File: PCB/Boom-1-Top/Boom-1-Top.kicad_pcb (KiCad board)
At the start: 2 copper layers, 310 parts, among them J37 Osc1Conn, J38 Osc2Conn, J39 SubNoiseConn, J40 FiltConn2, J41 EnvGenConn2, J42 EnvGenConn1, J43 FXConn1, J44 FiltConn1, J45 FXConn2, J46 EnvGenConn3, SW1 Rotary_Encoder, SW10 Rotary_Encoder, SW11 Rotary_Encoder, SW12 Rotary_Encoder, SW13 Rotary_Encoder, SW14 Rotary_Encoder, SW15 Rotary_Encoder_Switch, SW16 Rotary_Encoder_Switch, SW17 Rotary_Encoder, SW18 Rotary_Encoder, SW19 Rotary_Encoder, SW2 Rotary_Encoder, SW20 Rotary_Encoder, SW21 Rotary_Encoder, SW22 Rotary_Encoder, SW23 Rotary_Encoder, SW24 Rotary_Encoder, SW25 Rotary_Encoder, SW26 Rotary_Encoder, SW27 Rotary_Encoder, SW28 Rotary_Encoder_Switch, SW29 Rotary_Encoder, SW3 Rotary_Encoder, SW30 Rotary_Encoder, SW31 Rotary_Encoder, SW32 Rotary_Encoder, SW33 Rotary_Encoder, SW34 Rotary_Encoder, SW35 Rotary_Encoder, SW36 Rotary_Encoder, SW37 Rotary_Encoder, SW38 Rotary_Encoder, SW39 Rotary_Encoder, SW4 Rotary_Encoder, SW40 Rotary_Encoder, SW5 Rotary_Encoder, SW6 Rotary_Encoder, SW7 Rotary_Encoder, SW8 Rotary_Encoder, SW9 Rotary_Encoder, U1 STM32F407VGTx, U10 DAC7678xPW, U11 PIC18F26Q43, U12 PIC18F26Q43, U13 PIC18F26Q43, U14 PIC18F26Q43, U15 PIC18F26Q43, U16 PIC18F26Q43, U17 PIC18F26Q43, U18 PIC18F26Q43, U19 PIC18F26Q43, U2 PIC18F26Q43, U20 PIC18F26Q43, U3 AD5290, U4 AD5290, U5 DAC7678xPW, U6 DAC7678xPW, U7 DAC7678xPW, U8 DAC7678xPW, U9 DAC7678xPW

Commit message: Schematic WIP
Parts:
- added C100: 100nF, Capacitor_SMD:C_0603_1608Metric, F.Cu at (426.1, 310.0)
- added C101: 100nF, Capacitor_SMD:C_0603_1608Metric, F.Cu at (417.0, 317.2)
- added C102: 10uF, Capacitor_SMD:C_0603_1608Metric, F.Cu at (422.0, 312.5)
- added C103: 100nF, Capacitor_SMD:C_0603_1608Metric, F.Cu at (393.8, 341.5)
- added C104: 100nF, Capacitor_SMD:C_0603_1608Metric, F.Cu at (431.3, 304.9)
- added C105: 100nF, Capacitor_SMD:C_0603_1608Metric, F.Cu at (401.2, 332.8)
- added C106: 10nF, Capacitor_SMD:C_0603_1608Metric, F.Cu at (397.8, 325.3)
- added C107: 100nF, Capacitor_SMD:C_0603_1608Metric, F.Cu at (409.0, 316.8)
- added C108: 100nF, Capacitor_SMD:C_0603_1608Metric, F.Cu at (397.8, 327.8)
- added C109: 100nF, Capacitor_SMD:C_0603_1608Metric, F.Cu at (385.8, 340.3)
- added C110: 100nF, Capacitor_SMD:C_0603_1608Metric, F.Cu at (423.3, 302.4)
- added C111: 100nF, Capacitor_SMD:C_0603_1608Metric, F.Cu at (401.8, 325.3)
- added C112: 100nF, Capacitor_SMD:C_0603_1608Metric, F.Cu at (423.3, 304.9)
- added C113: 100nF, Capacitor_SMD:C_0603_1608Metric, F.Cu at (401.8, 327.8)
- added C114: 100nF, Capacitor_SMD:C_0603_1608Metric, F.Cu at (397.8, 330.3)
- added C115: 100nF, Capacitor_SMD:C_0603_1608Metric, F.Cu at (409.0, 319.4)
- added C116: 100nF, Capacitor_SMD:C_0603_1608Metric, F.Cu at (418.1, 309.6)
- added C117: 100nF, Capacitor_SMD:C_0603_1608Metric, F.Cu at (414.0, 312.2)
- added C118: 100nF, Capacitor_SMD:C_0603_1608Metric, F.Cu at (391.8, 336.5)
- added C119: 100nF, Capacitor_SMD:C_0603_1608Metric, F.Cu at (414.0, 314.7)
- added C120: 100nF, Capacitor_SMD:C_0603_1608Metric, F.Cu at (427.3, 302.4)
- added C121: 100nF, Capacitor_SMD:C_0603_1608Metric, F.Cu at (389.8, 339.2)
- added C122: 100nF, Capacitor_SMD:C_0603_1608Metric, F.Cu at (405.9, 325.3)
- added C123: 100nF, Capacitor_SMD:C_0603_1608Metric, F.Cu at (418.0, 312.2)
- added C124: 100nF, Capacitor_SMD:C_0603_1608Metric, F.Cu at (409.0, 321.9)
- added C125: 100nF, Capacitor_SMD:C_0603_1608Metric, F.Cu at (397.2, 332.8)
- added C126: 100nF, Capacitor_SMD:C_0603_1608Metric, F.Cu at (423.3, 307.5)
- added C127: 100nF, Capacitor_SMD:C_0603_1608Metric, F.Cu at (427.3, 304.9)
- added C128: 100nF, Capacitor_SMD:C_0603_1608Metric, F.Cu at (389.8, 341.7)
- added C129: 100nF, Capacitor_SMD:C_0603_1608Metric, F.Cu at (413.0, 317.2)
- added C130: 100nF, Capacitor_SMD:C_0603_1608Metric, F.Cu at (401.8, 330.3)
- added C131: 100nF, Capacitor_SMD:C_0603_1608Metric, F.Cu at (405.9, 327.8)
- added C132: 100nF, Capacitor_SMD:C_0603_1608Metric, F.Cu at (413.0, 319.8)
- added C133: 100nF, Capacitor_SMD:C_0603_1608Metric, F.Cu at (422.1, 310.0)
- added C134: 100nF, Capacitor_SMD:C_0603_1608Metric, F.Cu at (397.2, 335.3)
- added C135: 100nF, Capacitor_SMD:C_0603_1608Metric, F.Cu at (418.0, 314.7)
- added C136: 100nF, Capacitor_SMD:C_0603_1608Metric, F.Cu at (393.8, 339.0)
- added C137: 100nF, Capacitor_SMD:C_0603_1608Metric, F.Cu at (431.3, 302.4)
- added C138: 100nF, Capacitor_SMD:C_0603_1608Metric, F.Cu at (409.9, 324.4)
- added C81: 100nF, Capacitor_SMD:C_0603_1608Metric, F.Cu at (433.1, 317.5)
- added C82: 10uF, Capacitor_SMD:C_0603_1608Metric, F.Cu at (417.9, 332.3)
- added C83: 100nF, Capacitor_SMD:C_0603_1608Metric, F.Cu at (429.9, 320.0)
- added C84: 10uF, Capacitor_SMD:C_0603_1608Metric, F.Cu at (421.9, 327.5)
- added C85: 12pF, Capacitor_SMD:C_0603_1608Metric, F.Cu at (409.8, 339.4)
- added C86: 2.2uF, Capacitor_SMD:C_0603_1608Metric, F.Cu at (413.9, 334.8)
- added C87: 100nF, Capacitor_SMD:C_0603_1608Metric, F.Cu at (413.9, 324.8)
- added C88: 12pF, Capacitor_SMD:C_0603_1608Metric, F.Cu at (431.3, 307.5)
- added C89: 100nF, Capacitor_SMD:C_0603_1608Metric, F.Cu at (426.0, 312.5)
- added C90: 10uF, Capacitor_SMD:C_0603_1608Metric, F.Cu at (405.2, 332.8)
- added C91: 100nF, Capacitor_SMD:C_0603_1608Metric, F.Cu at (397.8, 340.4)
- added C92: 100nF, Capacitor_SMD:C_0603_1608Metric, F.Cu at (413.9, 322.3)
- added C93: 10uF, Capacitor_SMD:C_0603_1608Metric, F.Cu at (435.3, 302.4)
- added C94: 100nF, Capacitor_SMD:C_0603_1608Metric, F.Cu at (397.8, 337.8)
- added C95: 2.2uF, Capacitor_SMD:C_0603_1608Metric, F.Cu at (422.0, 315.0)
- added C96: 100nF, Capacitor_SMD:C_0603_1608Metric, F.Cu at (401.2, 335.3)
- added C97: 10uF, Capacitor_SMD:C_0603_1608Metric, F.Cu at (417.0, 319.8)
- added C98: 100nF, Capacitor_SMD:C_0603_1608Metric, F.Cu at (409.9, 326.9)
- added C99: 2.2uF, Capacitor_SMD:C_0603_1608Metric, F.Cu at (405.9, 330.3)
- added D1: B5819W, Diode_SMD:D_SOD-123, F.Cu at (375.1, 338.2)
- added D2: Red, LED_SMD:LED_0603_1608Metric, F.Cu at (414.1, 309.7)
- added D3: 1N4148, Diode_SMD:D_SOD-123, F.Cu at (380.9, 340.7)
- added F1: 500mA, Fuse:Fuse_0603_1608Metric, F.Cu at (427.3, 307.5)
- added FB1: 100R@100Mhz, Inductor_SMD:L_0805_2012Metric, F.Cu at (387.6, 336.6)
- added FB2: 100R@100Mhz, Inductor_SMD:L_0805_2012Metric, F.Cu at (374.6, 341.3)
- added J1: DEBUG, Connector_PinHeader_1.27mm:PinHeader_2x05_P1.27mm_Vertical_SMD, F.Cu at (402.5, 305.4)
- added J10: MCLRCap, Connector_PinHeader_2.54mm:PinHeader_1x02_P2.54mm_Vertical, F.Cu at (393.5, 325.6)
- added J11: MCLRCap, Connector_PinHeader_2.54mm:PinHeader_1x02_P2.54mm_Vertical, F.Cu at (404.7, 312.0)
- added J12: MCLRCap, Connector_PinHeader_2.54mm:PinHeader_1x02_P2.54mm_Vertical, F.Cu at (382.9, 334.1)
- added J13: MCLRCap, Connector_PinHeader_2.54mm:PinHeader_1x02_P2.54mm_Vertical, F.Cu at (409.7, 303.5)
- added J14: MCLRCap, Connector_PinHeader_2.54mm:PinHeader_1x02_P2.54mm_Vertical, F.Cu at (400.0, 312.0)
- added J2: MIDI IN, 5PINDIN:SWITCHCRAFT_57PC5F, F.Cu at (388.3, 312.0)
- added J3: MIDI OUT, 5PINDIN:SWITCHCRAFT_57PC5F, F.Cu at (370.7, 312.0)
- added J4: MCLRCap, Connector_PinHeader_2.54mm:PinHeader_1x02_P2.54mm_Vertical, F.Cu at (387.6, 330.3)
- added J5: MCLRCap, Connector_PinHeader_2.54mm:PinHeader_1x02_P2.54mm_Vertical, F.Cu at (419.0, 303.5)
- added J6: MCLRCap, Connector_PinHeader_2.54mm:PinHeader_1x02_P2.54mm_Vertical, F.Cu at (404.7, 319.2)
- added J7: MCLRCap, Connector_PinHeader_2.54mm:PinHeader_1x02_P2.54mm_Vertical, F.Cu at (409.7, 310.7)
- added J8: MCLRCap, Connector_PinHeader_2.54mm:PinHeader_1x02_P2.54mm_Vertical, F.Cu at (400.0, 319.2)
- added J9: MCLRCap, Connector_PinHeader_2.54mm:PinHeader_1x02_P2.54mm_Vertical, F.Cu at (414.3, 303.5)
- added R161: 220R, Resistor_SMD:R_0603_1608Metric, F.Cu at (435.3, 304.9)
- added R162: 2.2K, Resistor_SMD:R_0603_1608Metric, F.Cu at (417.9, 322.3)
- added R163: 10K, Resistor_SMD:R_0603_1608Metric, F.Cu at (401.8, 337.8)
- added R164: 10K, Resistor_SMD:R_0603_1608Metric, F.Cu at (421.0, 317.5)
- added R165: 2.2K, Resistor_SMD:R_0603_1608Metric, F.Cu at (409.9, 329.4)
- added R166: 2.2K, Resistor_SMD:R_0603_1608Metric, F.Cu at (430.1, 310.0)
- added R167: 2.2K, Resistor_SMD:R_0603_1608Metric, F.Cu at (405.2, 335.3)
- added R168: 2.2K, Resistor_SMD:R_0603_1608Metric, F.Cu at (426.0, 315.0)
- added R169: 220R, Resistor_SMD:R_0603_1608Metric, F.Cu at (409.9, 331.9)
- added R170: 220R, Resistor_SMD:R_0603_1608Metric, F.Cu at (413.9, 327.3)
- added R171: 10K, Resistor_SMD:R_0603_1608Metric, F.Cu at (401.8, 340.4)
- added R172: 470R, Resistor_SMD:R_0603_1608Metric, F.Cu at (430.1, 312.5)
- added R173: 470R, Resistor_SMD:R_0603_1608Metric, F.Cu at (435.3, 307.5)
- added R174: 470R, Resistor_SMD:R_0603_1608Metric, F.Cu at (425.1, 317.5)
- added R175: 10K, Resistor_SMD:R_0603_1608Metric, F.Cu at (417.9, 324.8)
- added R176: 10K, Resistor_SMD:R_0603_1608Metric, F.Cu at (413.9, 329.8)
- added R177: 10K, Resistor_SMD:R_0603_1608Metric, F.Cu at (409.2, 334.4)
- added R178: 470R, Resistor_SMD:R_0603_1608Metric, F.Cu at (434.1, 310.0)
- added R179: 470R, Resistor_SMD:R_0603_1608Metric, F.Cu at (405.8, 337.8)
- added R180: 10K, Resistor_SMD:R_0603_1608Metric, F.Cu at (421.9, 320.0)
- added R181: 10K, Resistor_SMD:R_0603_1608Metric, F.Cu at (421.9, 322.5)
- added R182: 470R, Resistor_SMD:R_0603_1608Metric, F.Cu at (430.1, 315.0)
- added R183: 470R, Resistor_SMD:R_0603_1608Metric, F.Cu at (417.9, 327.3)
- added R184: 10K, Resistor_SMD:R_0603_1608Metric, F.Cu at (405.8, 340.4)
- added R185: 10K, Resistor_SMD:R_0603_1608Metric, F.Cu at (425.9, 320.0)
- added R186: 470R, Resistor_SMD:R_0603_1608Metric, F.Cu at (434.1, 312.5)
- added R187: 10K, Resistor_SMD:R_0603_1608Metric, F.Cu at (413.9, 332.3)
- added R188: 470R, Resistor_SMD:R_0603_1608Metric, F.Cu at (429.1, 317.5)
- added R189: 470R, Resistor_SMD:R_0603_1608Metric, F.Cu at (417.9, 329.8)
- added R190: 10K, Resistor_SMD:R_0603_1608Metric, F.Cu at (421.9, 325.0)
- added R191: 10K, Resistor_SMD:R_0603_1608Metric, F.Cu at (409.8, 336.9)
- added R192: 470R, Resistor_SMD:R_0603_1608Metric, F.Cu at (425.9, 322.5)
- added R193: 10K, Resistor_SMD:R_0603_1608Metric, F.Cu at (434.1, 315.0)
- added SW41: Reset, Button_Switch_THT:SW_PUSH_6mm, F.Cu at (375.3, 325.3)
- added U21: AMS1117-3.3, Package_TO_SOT_SMD:SOT-223-3_TabPin2, F.Cu at (367.4, 339.1)
- added U22: 6N137, Package_DIP:DIP-8_W7.62mm, F.Cu at (364.1, 325.3)
- added U3: AD5290, Package_SO:MSOP-10_3x3mm_P0.5mm, F.Cu at (387.5, 325.6)
- added U4: AD5290, Package_SO:MSOP-10_3x3mm_P0.5mm, F.Cu at (376.9, 334.2)
- added Y1: 16Mhz, Crystal:Crystal_SMD_3225-4Pin_3.2x2.5mm, F.Cu at (392.6, 332.7)
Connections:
- U1 pad 10: Net-(U1-Pad10) -> GND
- U1 pad 100: Net-(U1-Pad100) -> +3V3
- U1 pad 11: Net-(U1-Pad11) -> +3V3
- U1 pad 12: Net-(U1-Pad12) -> HSE_IN
- U1 pad 13: Net-(U1-Pad13) -> HSE_OUT
- U1 pad 19: Net-(U1-Pad19) -> +3V3
- U1 pad 20: Net-(U1-Pad20) -> GND
- U1 pad 21: Net-(U1-Pad21) -> +3.3VA
- U1 pad 22: Net-(U1-Pad22) -> +3.3VA
- U1 pad 27: Net-(U1-Pad27) -> GND
- U1 pad 28: Net-(U1-Pad28) -> +3V3
- U1 pad 37: Net-(U1-Pad37) -> BOOT1
- U1 pad 50: Net-(U1-Pad50) -> +3V3
- U1 pad 6: Net-(U1-Pad6) -> +3V3
- U1 pad 72: Net-(U1-Pad72) -> SWDIO
- U1 pad 74: Net-(U1-Pad74) -> GND
- U1 pad 75: Net-(U1-Pad75) -> +3V3
- U1 pad 76: Net-(U1-Pad76) -> SWCLK
- U1 pad 89: Net-(U1-Pad89) -> SWO
- U1 pad 94: Net-(U1-Pad94) -> BOOT0
- U1 pad 99: Net-(U1-Pad99) -> GND
- U11 pad 19: Net-(U11-Pad19) -> GND
- U11 pad 20: Net-(U11-Pad20) -> +5V
- U11 pad 8: Net-(U11-Pad8) -> GND
- U12 pad 19: Net-(U12-Pad19) -> GND
- U12 pad 20: Net-(U12-Pad20) -> +5V
- U12 pad 8: Net-(U12-Pad8) -> GND
- U13 pad 19: Net-(U13-Pad19) -> GND
- U13 pad 20: Net-(U13-Pad20) -> +5V
- U13 pad 8: Net-(U13-Pad8) -> GND
- U14 pad 19: Net-(U14-Pad19) -> GND
- U14 pad 20: Net-(U14-Pad20) -> +5V
- U14 pad 8: Net-(U14-Pad8) -> GND
- U15 pad 19: Net-(U15-Pad19) -> GND
- U15 pad 20: Net-(U15-Pad20) -> +5V
- U15 pad 8: Net-(U15-Pad8) -> GND
- U16 pad 19: Net-(U16-Pad19) -> GND
- U16 pad 20: Net-(U16-Pad20) -> +5V
- U16 pad 8: Net-(U16-Pad8) -> GND
- U17 pad 19: Net-(U17-Pad19) -> GND
- U17 pad 20: Net-(U17-Pad20) -> +5V
- U17 pad 8: Net-(U17-Pad8) -> GND
- U18 pad 19: Net-(U18-Pad19) -> GND
- U18 pad 20: Net-(U18-Pad20) -> +5V
- U18 pad 8: Net-(U18-Pad8) -> GND
- U19 pad 19: Net-(U19-Pad19) -> GND
- U19 pad 20: Net-(U19-Pad20) -> +5V
- U19 pad 8: Net-(U19-Pad8) -> GND
- U2 pad 19: Net-(U2-Pad19) -> GND
- U2 pad 20: Net-(U2-Pad20) -> +5V
- U2 pad 8: Net-(U2-Pad8) -> GND
- U20 pad 19: Net-(U20-Pad19) -> GND
- U20 pad 20: Net-(U20-Pad20) -> +5V
- U20 pad 8: Net-(U20-Pad8) -> GND
- U5 pad 15: I2CBus1SDA -> I2CBus1SCL
- U5 pad 16: I2CBus1SCL -> Net-(U5-Pad16)

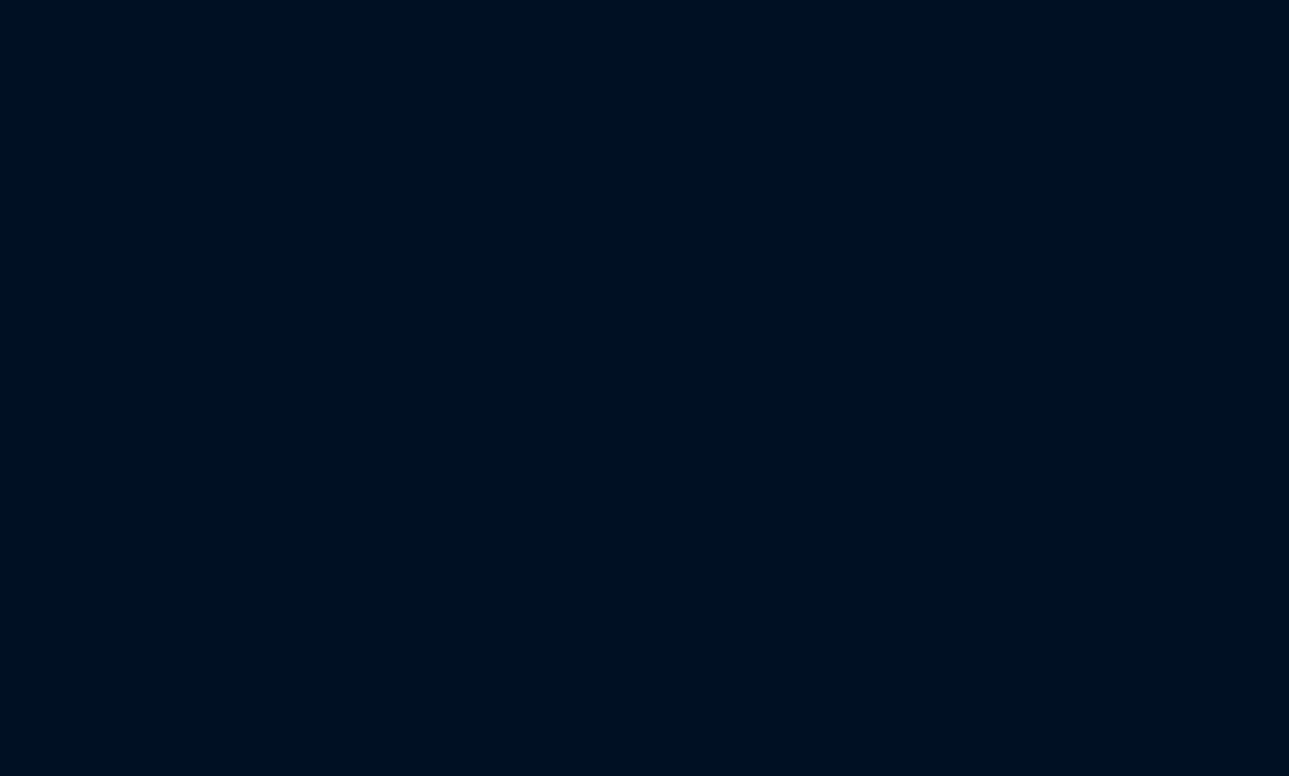
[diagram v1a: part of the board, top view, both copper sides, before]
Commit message: Annotated, set foot prints and updated PCB
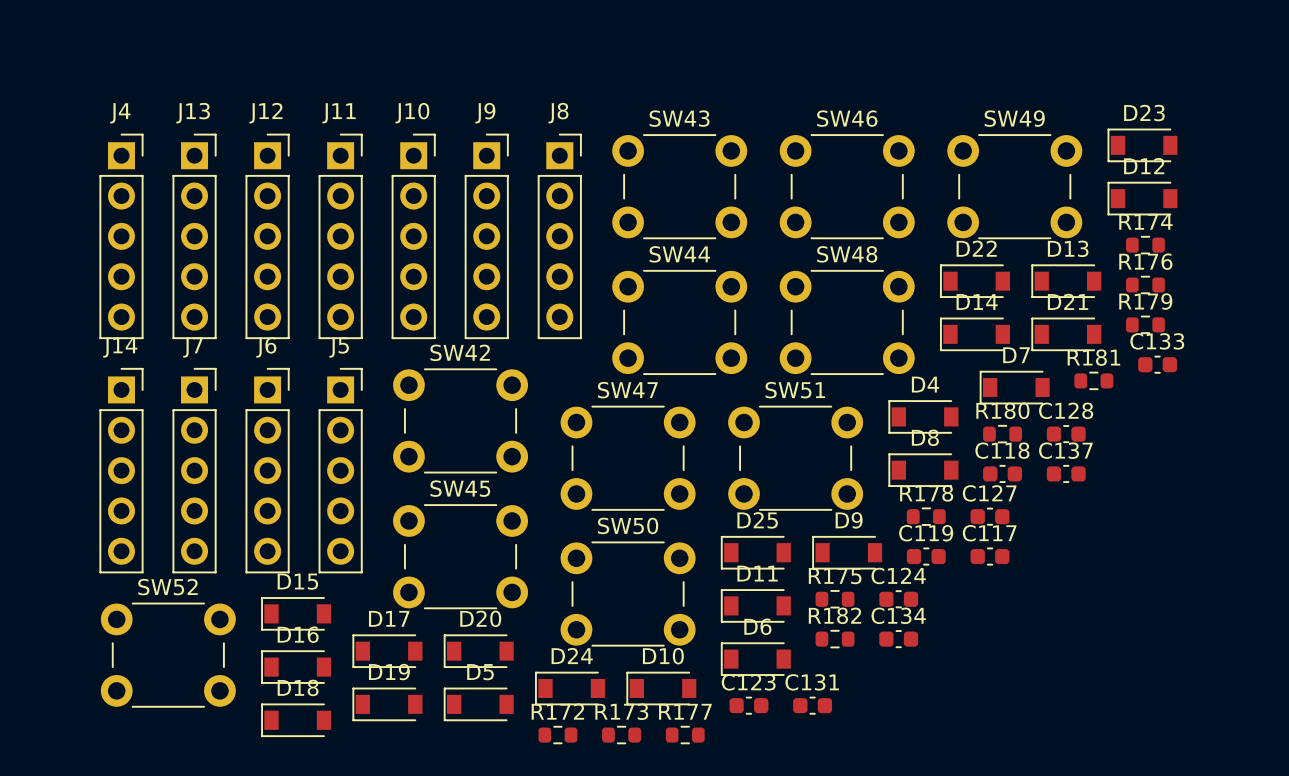
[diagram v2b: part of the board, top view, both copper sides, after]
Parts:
- added C117: 100nF, Capacitor_SMD:C_0603_1608Metric, F.Cu at (325.1, 365.8)
- added C118: 100nF, Capacitor_SMD:C_0603_1608Metric, F.Cu at (325.9, 360.6)
- added C119: 100nF, Capacitor_SMD:C_0603_1608Metric, F.Cu at (321.1, 365.8)
- added C123: 100nF, Capacitor_SMD:C_0603_1608Metric, F.Cu at (309.9, 375.1)
- added C124: 100nF, Capacitor_SMD:C_0603_1608Metric, F.Cu at (319.4, 368.4)
- added C127: 100nF, Capacitor_SMD:C_0603_1608Metric, F.Cu at (325.1, 363.2)
- added C128: 100nF, Capacitor_SMD:C_0603_1608Metric, F.Cu at (329.9, 358.1)
- added C131: 100nF, Capacitor_SMD:C_0603_1608Metric, F.Cu at (313.9, 375.1)
- added C133: 100nF, Capacitor_SMD:C_0603_1608Metric, F.Cu at (335.7, 353.7)
- added C134: 100nF, Capacitor_SMD:C_0603_1608Metric, F.Cu at (319.4, 371.0)
- added C137: 100nF, Capacitor_SMD:C_0603_1608Metric, F.Cu at (329.9, 360.6)
- added D10: B5819W, Diode_SMD:D_SOD-123, F.Cu at (304.5, 374.1)
- added D11: B5819W, Diode_SMD:D_SOD-123, F.Cu at (310.5, 368.9)
- added D12: B5819W, Diode_SMD:D_SOD-123, F.Cu at (334.8, 343.2)
- added D13: B5819W, Diode_SMD:D_SOD-123, F.Cu at (330.0, 348.4)
- added D14: B5819W, Diode_SMD:D_SOD-123, F.Cu at (324.3, 351.8)
- added D15: B5819W, Diode_SMD:D_SOD-123, F.Cu at (281.5, 369.4)
- added D16: B5819W, Diode_SMD:D_SOD-123, F.Cu at (281.5, 372.7)
- added D17: B5819W, Diode_SMD:D_SOD-123, F.Cu at (287.3, 371.7)
- added D18: B5819W, Diode_SMD:D_SOD-123, F.Cu at (281.5, 376.1)
- added D19: B5819W, Diode_SMD:D_SOD-123, F.Cu at (287.3, 375.1)
- added D20: B5819W, Diode_SMD:D_SOD-123, F.Cu at (293.0, 371.7)
- added D21: B5819W, Diode_SMD:D_SOD-123, F.Cu at (330.0, 351.8)
- added D22: B5819W, Diode_SMD:D_SOD-123, F.Cu at (324.3, 348.4)
- added D23: B5819W, Diode_SMD:D_SOD-123, F.Cu at (334.8, 339.9)
- added D24: B5819W, Diode_SMD:D_SOD-123, F.Cu at (298.8, 374.1)
- added D25: B5819W, Diode_SMD:D_SOD-123, F.Cu at (310.5, 365.5)
- added D4: B5819W, Diode_SMD:D_SOD-123, F.Cu at (321.0, 357.0)
- added D5: B5819W, Diode_SMD:D_SOD-123, F.Cu at (293.0, 375.1)
- added D6: B5819W, Diode_SMD:D_SOD-123, F.Cu at (310.5, 372.2)
- added D7: B5819W, Diode_SMD:D_SOD-123, F.Cu at (326.8, 355.1)
- added D8: B5819W, Diode_SMD:D_SOD-123, F.Cu at (321.0, 360.3)
- added D9: B5819W, Diode_SMD:D_SOD-123, F.Cu at (316.2, 365.5)
- added J10: PIC_DEBUG, Connector_PinSocket_2.54mm:PinSocket_1x05_P2.54mm_Vertical, F.Cu at (288.8, 340.5)
- added J11: PIC_DEBUG, Connector_PinSocket_2.54mm:PinSocket_1x05_P2.54mm_Vertical, F.Cu at (284.2, 340.5)
- added J12: PIC_DEBUG, Connector_PinSocket_2.54mm:PinSocket_1x05_P2.54mm_Vertical, F.Cu at (279.6, 340.5)
- added J13: PIC_DEBUG, Connector_PinSocket_2.54mm:PinSocket_1x05_P2.54mm_Vertical, F.Cu at (275.0, 340.5)
- added J14: PIC_DEBUG, Connector_PinSocket_2.54mm:PinSocket_1x05_P2.54mm_Vertical, F.Cu at (270.4, 355.3)
- added J4: PIC_DEBUG, Connector_PinSocket_2.54mm:PinSocket_1x05_P2.54mm_Vertical, F.Cu at (270.4, 340.5)
- added J5: PIC_DEBUG, Connector_PinSocket_2.54mm:PinSocket_1x05_P2.54mm_Vertical, F.Cu at (284.2, 355.3)
- added J6: PIC_DEBUG, Connector_PinSocket_2.54mm:PinSocket_1x05_P2.54mm_Vertical, F.Cu at (279.6, 355.3)
- added J7: PIC_DEBUG, Connector_PinSocket_2.54mm:PinSocket_1x05_P2.54mm_Vertical, F.Cu at (275.0, 355.3)
- added J8: PIC_DEBUG, Connector_PinSocket_2.54mm:PinSocket_1x05_P2.54mm_Vertical, F.Cu at (298.0, 340.5)
- added J9: PIC_DEBUG, Connector_PinSocket_2.54mm:PinSocket_1x05_P2.54mm_Vertical, F.Cu at (293.4, 340.5)
- added R172: 10K, Resistor_SMD:R_0603_1608Metric, F.Cu at (297.9, 377.0)
- added R173: 10K, Resistor_SMD:R_0603_1608Metric, F.Cu at (301.9, 377.0)
- added R174: 10K, Resistor_SMD:R_0603_1608Metric, F.Cu at (334.9, 346.1)
- added R175: 10K, Resistor_SMD:R_0603_1608Metric, F.Cu at (315.4, 368.4)
- added R176: 10K, Resistor_SMD:R_0603_1608Metric, F.Cu at (334.9, 348.7)
- added R177: 10K, Resistor_SMD:R_0603_1608Metric, F.Cu at (305.9, 377.0)
- added R178: 10K, Resistor_SMD:R_0603_1608Metric, F.Cu at (321.1, 363.2)
- added R179: 10K, Resistor_SMD:R_0603_1608Metric, F.Cu at (334.9, 351.2)
- added R180: 10K, Resistor_SMD:R_0603_1608Metric, F.Cu at (325.9, 358.1)
- added R181: 10K, Resistor_SMD:R_0603_1608Metric, F.Cu at (331.7, 354.7)
- added R182: 10K, Resistor_SMD:R_0603_1608Metric, F.Cu at (315.4, 371.0)
- added SW42: Reset, Button_Switch_THT:SW_PUSH_6mm, F.Cu at (288.5, 355.0)
- added SW43: Reset, Button_Switch_THT:SW_PUSH_6mm, F.Cu at (302.3, 340.2)
- added SW44: Reset, Button_Switch_THT:SW_PUSH_6mm, F.Cu at (302.3, 348.8)
- added SW45: Reset, Button_Switch_THT:SW_PUSH_6mm, F.Cu at (288.5, 363.5)
- added SW46: Reset, Button_Switch_THT:SW_PUSH_6mm, F.Cu at (312.9, 340.2)
- added SW47: Reset, Button_Switch_THT:SW_PUSH_6mm, F.Cu at (299.1, 357.3)
- added SW48: Reset, Button_Switch_THT:SW_PUSH_6mm, F.Cu at (312.9, 348.8)
- added SW49: Reset, Button_Switch_THT:SW_PUSH_6mm, F.Cu at (323.4, 340.2)
- added SW50: Reset, Button_Switch_THT:SW_PUSH_6mm, F.Cu at (299.1, 365.9)
- added SW51: Reset, Button_Switch_THT:SW_PUSH_6mm, F.Cu at (309.6, 357.3)
- added SW52: Reset, Button_Switch_THT:SW_PUSH_6mm, F.Cu at (270.1, 369.7)
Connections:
- R102 pad 1: Net-(R102-Pad1) -> +5V
- R58 pad 1: Net-(R58-Pad1) -> +5V
- R78 pad 1: Net-(R78-Pad1) -> +5V
- R86 pad 1: Net-(R86-Pad1) -> +5V
- SW15 pad S1: Net-(SW15-PadS1) -> GND
- SW16 pad S1: Net-(SW16-PadS1) -> GND
- SW28 pad S2: Net-(SW28-PadS2) -> GND
- U1 pad 25: Net-(U1-Pad25) -> MIDITXUSART
- U1 pad 30: Net-(U1-Pad30) -> SPIBus1CLK
- U1 pad 31: Net-(U1-Pad31) -> SPIBus1SDO
- U1 pad 32: Net-(U1-Pad32) -> SPIBus1SDI
- U1 pad 33: Net-(U1-Pad33) -> Osc1ScaleDPotCS
- U1 pad 34: Net-(U1-Pad34) -> Osc2ScaleDPotCS
- U1 pad 40: Net-(U1-Pad40) -> Osc1TuningOut
- U1 pad 42: Net-(U1-Pad42) -> Osc2TuningOut
- U1 pad 47: Net-(U1-Pad47) -> I2CBus2SCL
- U1 pad 48: Net-(U1-Pad48) -> I2CBus2SDA
- U1 pad 55: Net-(U1-Pad55) -> SubAmpEnvGate
- U1 pad 56: Net-(U1-Pad56) -> SubAmpEnvTrigger
- U1 pad 57: Net-(U1-Pad57) -> OscFiltEnv2Gate
- U1 pad 58: Net-(U1-Pad58) -> OscFiltEnv2Trigger
- U1 pad 59: Net-(U1-Pad59) -> OscFiltEnv1Gate
- U1 pad 60: Net-(U1-Pad60) -> OscFiltEnv1Trigger
- U1 pad 87: Net-(U1-Pad87) -> MIDIRXUSART
- U1 pad 92: Net-(U1-Pad92) -> I2CBus1SCL
- U1 pad 93: Net-(U1-Pad93) -> I2CBus1SDA
- U11 pad 1: Net-(R173-Pad2) -> Net-(D5-Pad1)
- U11 pad 15: Net-(U11-Pad15) -> Net-(C7-Pad2)
- U11 pad 16: Net-(U11-Pad16) -> Net-(C8-Pad1)
- U11 pad 17: Net-(U11-Pad17) -> Net-(C9-Pad2)
- U11 pad 18: Net-(U11-Pad18) -> Net-(C10-Pad1)
- U11 pad 2: Net-(U11-Pad2) -> Net-(C5-Pad2)
- U11 pad 21: Net-(U11-Pad21) -> I2CBus1SCL
- U11 pad 22: Net-(U11-Pad22) -> I2CBus1SDA
- U11 pad 3: Net-(U11-Pad3) -> Net-(C6-Pad1)
- U11 pad 4: Net-(U11-Pad4) -> Net-(C17-Pad2)
- U11 pad 5: Net-(U11-Pad5) -> Net-(C18-Pad1)
- U12 pad 1: Net-(R174-Pad2) -> Net-(D9-Pad1)
- U12 pad 15: Net-(U12-Pad15) -> Net-(C13-Pad2)
- U12 pad 16: Net-(U12-Pad16) -> Net-(C14-Pad1)
- U12 pad 2: Net-(U12-Pad2) -> Net-(C11-Pad2)
- U12 pad 21: Net-(U12-Pad21) -> I2CBus1SCL
- U12 pad 22: Net-(U12-Pad22) -> I2CBus1SDA
- U12 pad 3: Net-(U12-Pad3) -> Net-(C12-Pad1)
- U12 pad 4: Net-(U12-Pad4) -> Net-(C20-Pad1)
- U12 pad 5: Net-(U12-Pad5) -> Net-(C19-Pad2)
- U13 pad 1: Net-(R178-Pad2) -> Net-(D11-Pad1)
- U13 pad 15: Net-(U13-Pad15) -> Net-(C36-Pad2)
- U13 pad 16: Net-(U13-Pad16) -> Net-(C33-Pad1)
- U13 pad 2: Net-(U13-Pad2) -> Net-(C23-Pad2)
- U13 pad 21: Net-(U13-Pad21) -> I2CBus1SCL
- U13 pad 22: Net-(U13-Pad22) -> I2CBus1SDA
- U13 pad 3: Net-(U13-Pad3) -> Net-(C24-Pad1)
- U13 pad 4: Net-(U13-Pad4) -> Net-(C49-Pad2)
- U13 pad 5: Net-(U13-Pad5) -> Net-(C47-Pad1)
- U14 pad 1: Net-(R179-Pad2) -> Net-(D14-Pad1)
- U14 pad 15: Net-(U14-Pad15) -> Net-(C37-Pad2)
- U14 pad 16: Net-(U14-Pad16) -> Net-(C34-Pad1)
- U14 pad 17: Net-(U14-Pad17) -> Net-(C55-Pad2)
- U14 pad 18: Net-(U14-Pad18) -> Net-(C56-Pad1)
- U14 pad 2: Net-(U14-Pad2) -> Net-(C25-Pad2)
- U14 pad 21: Net-(U14-Pad21) -> I2CBus1SCL
- U14 pad 22: Net-(U14-Pad22) -> I2CBus1SDA
- U14 pad 3: Net-(U14-Pad3) -> Net-(C26-Pad1)
- U14 pad 4: Net-(U14-Pad4) -> Net-(C50-Pad2)
- U14 pad 5: Net-(U14-Pad5) -> Net-(C48-Pad1)
- U14 pad 9: Net-(U14-Pad9) -> Net-(SW28-PadS1)
- U15 pad 1: Net-(R182-Pad2) -> Net-(D15-Pad1)
- U15 pad 15: Net-(U15-Pad15) -> Net-(C41-Pad2)
- U15 pad 16: Net-(U15-Pad16) -> Net-(C39-Pad1)
- U15 pad 17: Net-(U15-Pad17) -> Net-(C53-Pad2)
- U15 pad 18: Net-(U15-Pad18) -> Net-(C51-Pad1)
- U15 pad 2: Net-(U15-Pad2) -> Net-(C31-Pad2)
- U15 pad 21: Net-(U15-Pad21) -> I2CBus1SCL
- U15 pad 22: Net-(U15-Pad22) -> I2CBus1SDA
- U15 pad 3: Net-(U15-Pad3) -> Net-(C29-Pad1)
- U15 pad 4: Net-(U15-Pad4) -> Net-(C45-Pad2)
- U15 pad 5: Net-(U15-Pad5) -> Net-(C43-Pad1)
- U15 pad 9: Net-(U15-Pad9) -> Net-(SW15-PadS2)
- U16 pad 1: Net-(R183-Pad2) -> Net-(D17-Pad1)
- U16 pad 15: Net-(U16-Pad15) -> Net-(C42-Pad2)
- U16 pad 16: Net-(U16-Pad16) -> Net-(C40-Pad1)
- U16 pad 17: Net-(U16-Pad17) -> Net-(C54-Pad2)
- U16 pad 18: Net-(U16-Pad18) -> Net-(C52-Pad1)
- U16 pad 2: Net-(U16-Pad2) -> Net-(C32-Pad2)
- U16 pad 21: Net-(U16-Pad21) -> I2CBus2SCL
- U16 pad 22: Net-(U16-Pad22) -> I2CBus2SDA
- U16 pad 3: Net-(U16-Pad3) -> Net-(C30-Pad1)
- U16 pad 4: Net-(U16-Pad4) -> Net-(C46-Pad2)
- U16 pad 5: Net-(U16-Pad5) -> Net-(C44-Pad1)
- U16 pad 9: Net-(U16-Pad9) -> Net-(SW16-PadS2)
- U17 pad 1: Net-(R186-Pad2) -> Net-(D19-Pad1)
- U17 pad 15: Net-(U17-Pad15) -> Net-(C35-Pad2)
- U17 pad 16: Net-(U17-Pad16) -> Net-(C38-Pad1)
- U17 pad 2: Net-(U17-Pad2) -> Net-(C27-Pad2)
- U17 pad 21: Net-(U17-Pad21) -> I2CBus2SCL
- U17 pad 22: Net-(U17-Pad22) -> I2CBus2SDA
- U17 pad 3: Net-(U17-Pad3) -> Net-(C28-Pad1)
- U18 pad 1: Net-(R188-Pad2) -> Net-(D24-Pad1)
- U18 pad 15: Net-(U18-Pad15) -> Net-(C62-Pad2)
- U18 pad 16: Net-(U18-Pad16) -> Net-(C65-Pad1)
- U18 pad 17: Net-(U18-Pad17) -> Net-(C75-Pad2)
- U18 pad 18: Net-(U18-Pad18) -> Net-(C77-Pad1)
- U18 pad 2: Net-(U18-Pad2) -> Net-(C57-Pad2)
- U18 pad 21: Net-(U18-Pad21) -> I2CBus2SCL
- U18 pad 22: Net-(U18-Pad22) -> I2CBus2SDA
- U18 pad 3: Net-(U18-Pad3) -> Net-(C59-Pad1)
- U18 pad 4: Net-(U18-Pad4) -> Net-(C69-Pad2)
- U18 pad 5: Net-(U18-Pad5) -> Net-(C72-Pad1)
- U19 pad 1: Net-(R189-Pad2) -> Net-(D23-Pad1)
- U19 pad 15: Net-(U19-Pad15) -> Net-(C66-Pad2)
- U19 pad 16: Net-(U19-Pad16) -> Net-(C64-Pad1)
- U19 pad 17: Net-(U19-Pad17) -> Net-(C78-Pad2)
- U19 pad 18: Net-(U19-Pad18) -> Net-(C76-Pad1)
- U19 pad 2: Net-(U19-Pad2) -> Net-(C60-Pad2)
- U19 pad 21: Net-(U19-Pad21) -> I2CBus2SCL
- U19 pad 22: Net-(U19-Pad22) -> I2CBus2SDA
- U19 pad 4: Net-(U19-Pad4) -> Net-(C73-Pad2)
- U19 pad 5: Net-(U19-Pad5) -> Net-(C70-Pad1)
- U2 pad 1: Net-(R172-Pad2) -> Net-(D7-Pad1)
- U2 pad 11: Net-(C1-Pad2) -> Net-(U2-Pad11)
- U2 pad 12: Net-(C2-Pad1) -> Net-(U2-Pad12)
- U2 pad 13: Net-(C3-Pad2) -> Net-(U2-Pad13)
- U2 pad 14: Net-(C4-Pad1) -> Net-(U2-Pad14)
- U2 pad 15: Net-(C15-Pad2) -> Net-(C3-Pad2)
- U2 pad 16: Net-(C16-Pad1) -> Net-(C4-Pad1)
- U2 pad 2: Net-(U2-Pad2) -> Net-(C1-Pad2)
- U2 pad 21: Net-(U2-Pad21) -> I2CBus1SCL
- U2 pad 22: Net-(U2-Pad22) -> I2CBus1SDA
- U2 pad 3: Net-(U2-Pad3) -> Net-(C2-Pad1)
- U2 pad 4: Net-(U2-Pad4) -> Net-(C15-Pad2)
- U2 pad 5: Net-(U2-Pad5) -> Net-(C16-Pad1)
- U20 pad 1: Net-(R192-Pad2) -> Net-(D25-Pad1)
- U20 pad 15: Net-(U20-Pad15) -> Net-(C68-Pad2)
- U20 pad 16: Net-(U20-Pad16) -> Net-(C67-Pad1)
- U20 pad 17: Net-(U20-Pad17) -> Net-(C80-Pad2)
- U20 pad 18: Net-(U20-Pad18) -> Net-(C79-Pad1)
- U20 pad 2: Net-(U20-Pad2) -> Net-(C63-Pad2)
- U20 pad 21: Net-(U20-Pad21) -> I2CBus2SCL
- U20 pad 22: Net-(U20-Pad22) -> I2CBus2SDA
- U20 pad 3: Net-(U20-Pad3) -> Net-(C61-Pad1)
- U20 pad 4: Net-(U20-Pad4) -> Net-(C74-Pad2)
- U20 pad 5: Net-(U20-Pad5) -> Net-(C71-Pad1)

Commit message: Headers layed out
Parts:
- J37, J38, J39, J40, J41, J42, J43, J44, J45, J46: moved to B.Cu
- moved J3 385.5 mm to (123.7, 16.0)
- moved J2 385.5 mm to (141.3, 16.0)
- moved J44 294.9 mm to (129.0, 34.5), turned to 270 degrees
- moved SW8 281.4 mm to (90.0, 64.0)
- moved SW1 275.1 mm to (76.0, 32.0)
- moved SW9 272.3 mm to (90.0, 114.0)
- moved J45 265.3 mm to (269.0, 34.5), turned to 270 degrees
- moved SW2 262.7 mm to (76.0, 49.0)
- moved SW15 261.6 mm to (150.0, 79.0)
- moved SW17 256.1 mm to (171.0, 53.0)
- moved J37 255.2 mm to (39.0, 64.0), turned to 180 degrees
- moved SW4 254.0 mm to (76.0, 105.0)
- moved SW3 249.9 mm to (76.0, 88.0)
- moved SW13 246.5 mm to (140.0, 106.0)
- moved SW24 241.6 mm to (202.0, 53.0)
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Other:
- board outline added: 345 x 165 mm
